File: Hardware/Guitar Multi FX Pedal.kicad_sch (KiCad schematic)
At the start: 0 parts

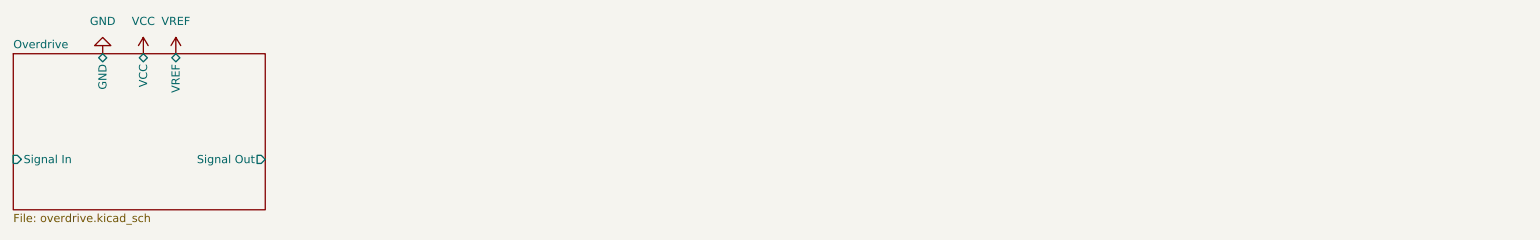
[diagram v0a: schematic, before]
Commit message: Add Octaver and Reverb effects
Added the schematics for the octaver and reverb effects, also fixed up some minor things on the overdrive schematic.
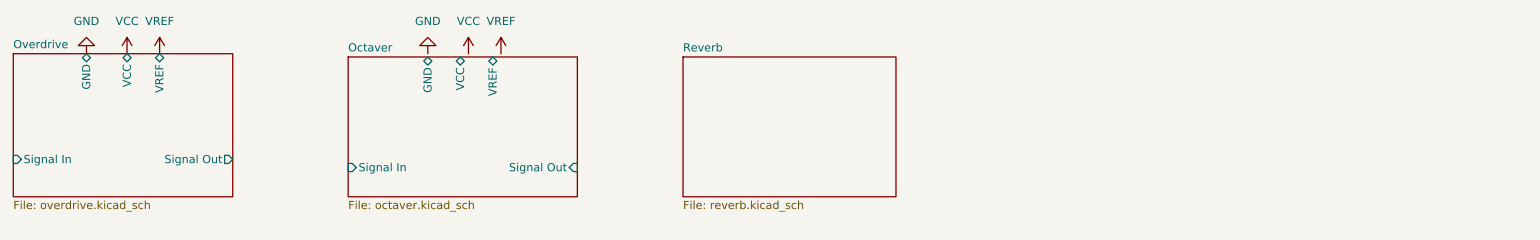
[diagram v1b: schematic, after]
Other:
- added sheet Octaver (octaver.kicad_sch)
- added sheet Reverb (reverb.kicad_sch)

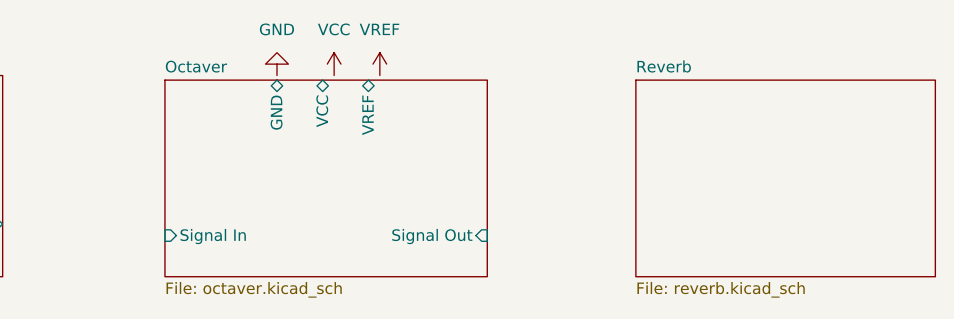
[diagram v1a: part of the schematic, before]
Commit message: Add power symbols to Reverb
Added proper power connections to the reverb sub sheet, and connections to the global schematic.
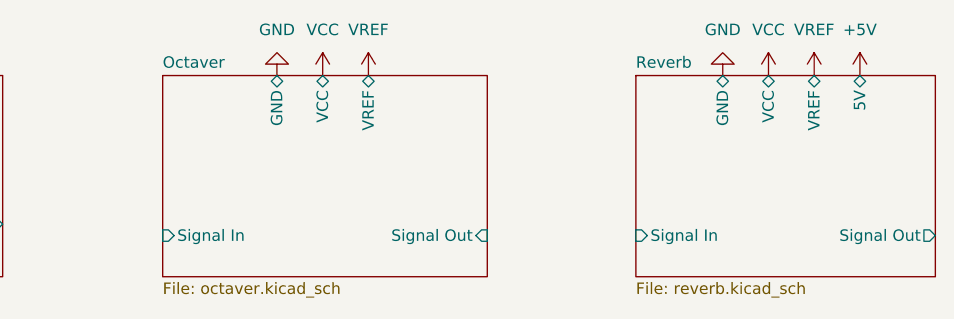
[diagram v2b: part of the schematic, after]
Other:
- sheet Reverb ports: added 5V, GND, Signal In, Signal Out, VCC, VREF; removed none

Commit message: Add chorus
Added the schematic for the chorus effect
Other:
- added sheet Chorus (chorus.kicad_sch)
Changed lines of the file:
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@@
+		)
+	)
+	(sheet
+		(at 175.006 21.336)
+		(size 41.402 22.606)
+		(exclude_from_sim no)
+		(in_bom yes)
+		(on_board yes)
+		(dnp no)
+		(fields_autoplaced yes)
+		(stroke
+			(width 0.1524)
+			(type solid)
+		)
+		(fill
+			(color 0 0 0 0.0000)
+		)
+		(property "Sheetname" "Chorus"
+			(at 175.006 20.6244 0)
+			(effects
+				(font
+					(size 1.27 1.27)
+				)
+				(justify left bottom)
+			)
+		)
+		(property "Sheetfile" "chorus.kicad_sch"
+			(at 175.006 44.5266 0)
+			(effects
+				(font
+					(size 1.27 1.27)
+				)
+				(justify left top)
+			)
+		)
+		(instances
+			(project "Guitar Multi FX Pedal"
+				(path "/0ad2f1fd-76fe-43da-85d9-356ef89f741a"
+					(page "5")
+				)
+			)
 		)
 	)

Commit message: Add delay
Added the schematic for the delay effect
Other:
- added sheet Delay (delay.kicad_sch)
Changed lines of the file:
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@@
+	)
+	(sheet
+		(at 228.6 22.606)
+		(size 32.004 21.844)
+		(exclude_from_sim no)
+		(in_bom yes)
+		(on_board yes)
+		(dnp no)
+		(fields_autoplaced yes)
+		(stroke
+			(width 0.1524)
+			(type solid)
+		)
+		(fill
+			(color 0 0 0 0.0000)
+		)
+		(property "Sheetname" "Delay"
+			(at 228.6 21.8944 0)
+			(effects
+				(font
+					(size 1.27 1.27)
+				)
+				(justify left bottom)
+			)
+		)
+		(property "Sheetfile" "delay.kicad_sch"
+			(at 228.6 45.0346 0)
+			(effects
+				(font
+					(size 1.27 1.27)
+				)
+				(justify left top)
+			)
+		)
+		(instances
+			(project "Guitar Multi FX Pedal"
+				(path "/0ad2f1fd-76fe-43da-85d9-356ef89f741a"
+					(page "6")
+				)
+			)
+		)
 	)
 	(sheet
